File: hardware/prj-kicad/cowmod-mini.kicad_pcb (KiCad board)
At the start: 4 copper layers, 80 x 50 mm, 24 parts, among them P1 PMOD, P2 PMOD, U1 STM32F750V8, U2 ICE40HX1K-VQ100

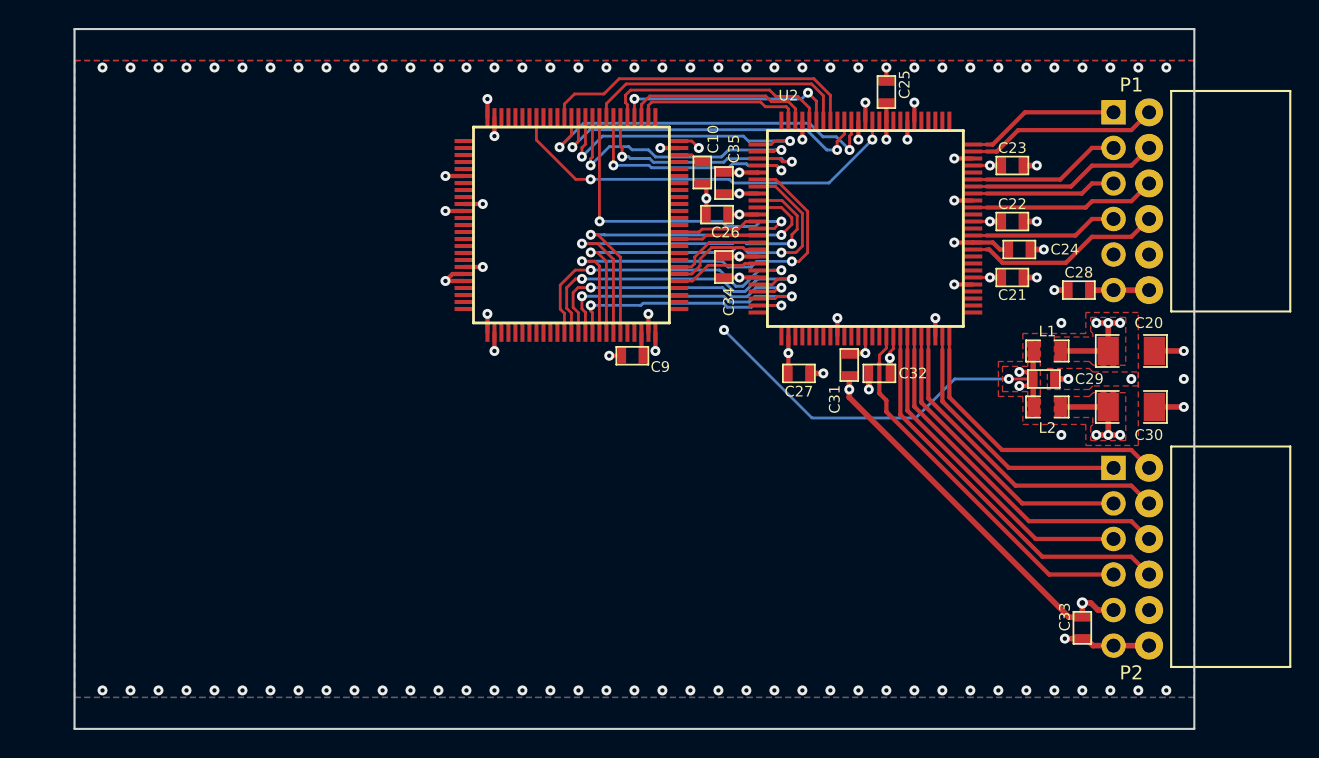
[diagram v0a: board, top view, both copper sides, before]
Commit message: = ADD: Insert ethernet network interface
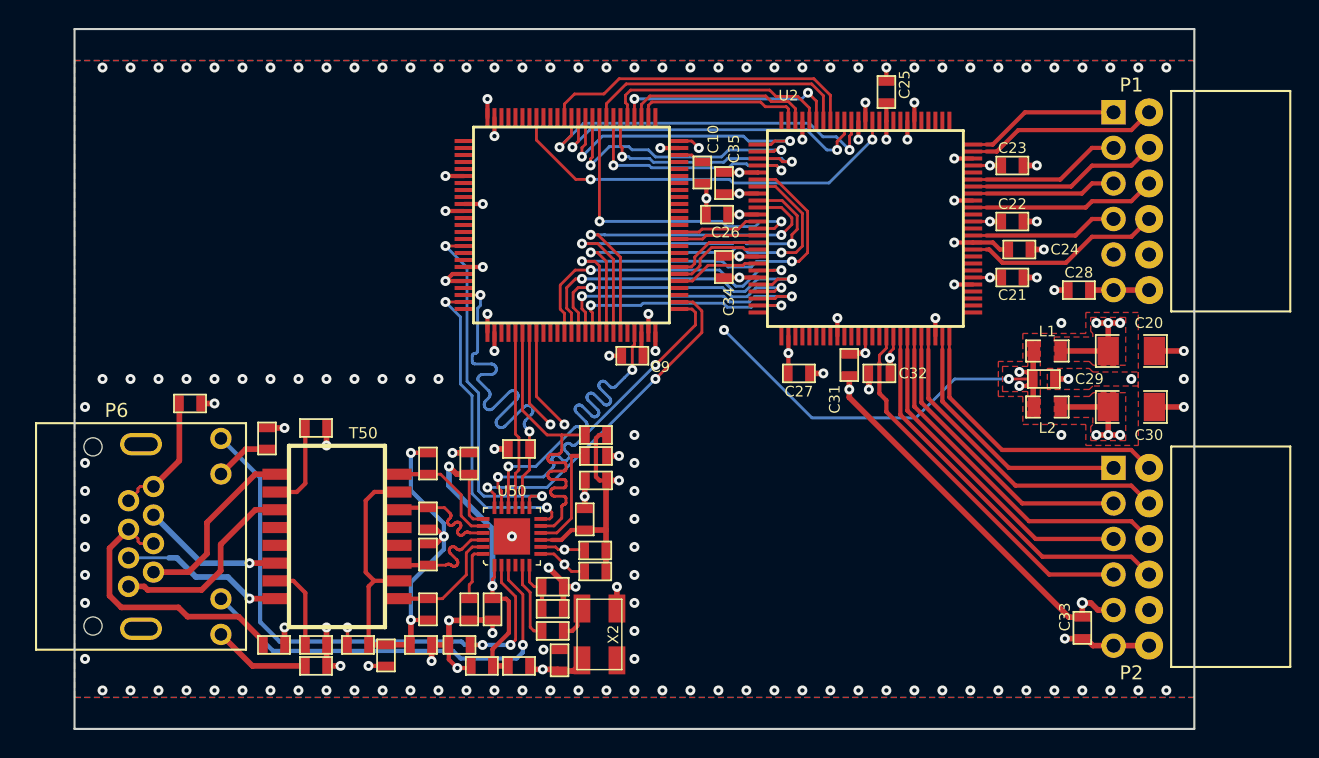
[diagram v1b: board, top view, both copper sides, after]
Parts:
- added C50: 100nF, cartes_v3:SMD0603, F.Cu at (143.2, 125.1)
- added C51: 100nF, cartes_v3:SMD0603, F.Cu at (133.2, 124.0)
- added C52: 100nF, cartes_v3:SMD0603, F.Cu at (128.8, 124.0)
- added C53: 470pF, cartes_v3:SMD0603, F.Cu at (142.7, 119.8)
- added C54: 1uF, cartes_v3:SMD0603, F.Cu at (142.7, 121.4)
- added C55: 1uF, cartes_v3:SMD0603, F.Cu at (137.6, 125.5)
- added C56: 100nF, cartes_v3:SMD0603, F.Cu at (138.4, 121.5)
- added C57: 100nF, cartes_v3:SMD0603, F.Cu at (136.7, 111.0)
- added C58: 1uF, cartes_v3:SMD0603, F.Cu at (145.8, 112.2)
- added C59: 100nF, cartes_v3:SMD0603, F.Cu at (144.9, 115.0)
- added L50: FB100, cartes_v3:SMD0603, F.Cu at (130.8, 124.8)
- added L51: FB120, cartes_v3:SMD0603, F.Cu at (140.2, 125.5)
- added P6: CONN_RJ45, cartes_v3:CONN_615008185121, F.Cu at (113.2, 116.2)
- added R50: 12.1k, cartes_v3:R_0603, F.Cu at (136.7, 121.5)
- added R51: 49.9, cartes_v3:SMD0603, F.Cu at (133.8, 121.5)
- added R52: 49.9, cartes_v3:SMD0603, F.Cu at (133.8, 117.5)
- added R53: 49.9, cartes_v3:SMD0603, F.Cu at (133.8, 115.0)
- added R54: 49.9, cartes_v3:SMD0603, F.Cu at (133.8, 111.0)
- added R55: 75, cartes_v3:SMD0603, F.Cu at (125.8, 108.5)
- added R56: 75, cartes_v3:SMD0603, F.Cu at (125.8, 124.0)
- added R57: 75, cartes_v3:SMD0603, F.Cu at (122.8, 124.0)
- added R58: 75, cartes_v3:SMD0603, F.Cu at (116.8, 106.8)
- added R59: 49.9, cartes_v3:R_0603, F.Cu at (142.7, 123.0)
- added R60: 4.7k, cartes_v3:R_0603, F.Cu at (145.7, 117.2)
- added R61: 4.7k, cartes_v3:R_0603, F.Cu at (145.7, 118.8)
- added R62: 4.7k, cartes_v3:R_0603, F.Cu at (145.8, 109.0)
- added R63: 4.7k, cartes_v3:R_0603, F.Cu at (145.8, 110.5)
- added R64: 4.7k, cartes_v3:R_0603, F.Cu at (140.2, 110.0)
- added R65: 4.7k, cartes_v3:R_0603, F.Cu at (136.0, 124.0)
- added R66: 330, cartes_v3:R_0603, F.Cu at (122.2, 109.2)
- added R67: 330, cartes_v3:R_0603, F.Cu at (125.8, 125.5)
- added T50: TRANSFORMER_1:1, cartes_v3:TR_W749013011, F.Cu at (127.2, 116.2)
- added U50: LAN8742A, cartes_v3:QFN24, F.Cu at (139.8, 116.2)
- added X2: 25MHz, cartes_v3:Q_SMD5x3, F.Cu at (146.0, 123.2)
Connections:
- U1 pad 16: Net-(U1-Pad16) -> ETH_MDC
- U1 pad 23: Net-(U1-Pad23) -> ETH_REF_CLK
- U1 pad 24: Net-(U1-Pad24) -> ETH_MDIO
- U1 pad 30: Net-(U1-Pad30) -> ETH_RST
- U1 pad 31: Net-(U1-Pad31) -> ETH_CRS_DV
- U1 pad 32: Net-(U1-Pad32) -> ETH_RXD0
- U1 pad 33: Net-(U1-Pad33) -> ETH_RXD1
- U1 pad 47: Net-(U1-Pad47) -> ETH_TXEN
- U1 pad 51: Net-(U1-Pad51) -> ETH_TXD0
- U1 pad 52: Net-(U1-Pad52) -> ETH_TXD1
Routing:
- net GND: track 434.3 -> 638.3 mm, vias 112 -> 161
- net +3.3V: track 135.4 -> 214.1 mm, vias 15 -> 19
- net NET_LED2: track 0.00 -> 40.0 mm, vias 0 -> 2
- net Net-(C51-Pad1): track 0.00 -> 38.9 mm, vias 0 -> 3
- net NET_LED1: track 0.00 -> 30.2 mm, vias 0 -> 1
- net ETH_REF_CLK: track 0.00 -> 29.4 mm, vias 0 -> 2
- net ETH_RXD1: track 0.00 -> 28.7 mm, vias 0 -> 2
- net ETH_RXD0: track 0.00 -> 28.4 mm, vias 0 -> 2
- net ETH_MDC: track 0.00 -> 26.1 mm, vias 0 -> 2
- net Net-(C55-Pad1): track 0.00 -> 25.5 mm, vias 0 -> 2
- net ETH_TXD0: track 0.00 -> 25.0 mm, vias 0 -> 2
- net ETH_TXD1: track 0.00 -> 25.0 mm, vias 0 -> 2
- net ETH_TXEN: track 0.00 -> 25.0 mm, vias 0 -> 2
- net ETH_CRS_DV: track 0.00 -> 24.5 mm
- net ETH_MDIO: track 0.00 -> 23.2 mm, vias 0 -> 2
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- added copper zone on In2.Cu, net +3.3V
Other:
- net class Default: via_dia 0.8 -> 0.6
- rule solder_mask_min_width: 0.25 -> 0.05
- rule trace_min: 0.2032 -> 0.1524
- board text removed: "PWR"

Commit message: = ADD: Insert power supply regulators (3V3 / 1V2 / 2V5)
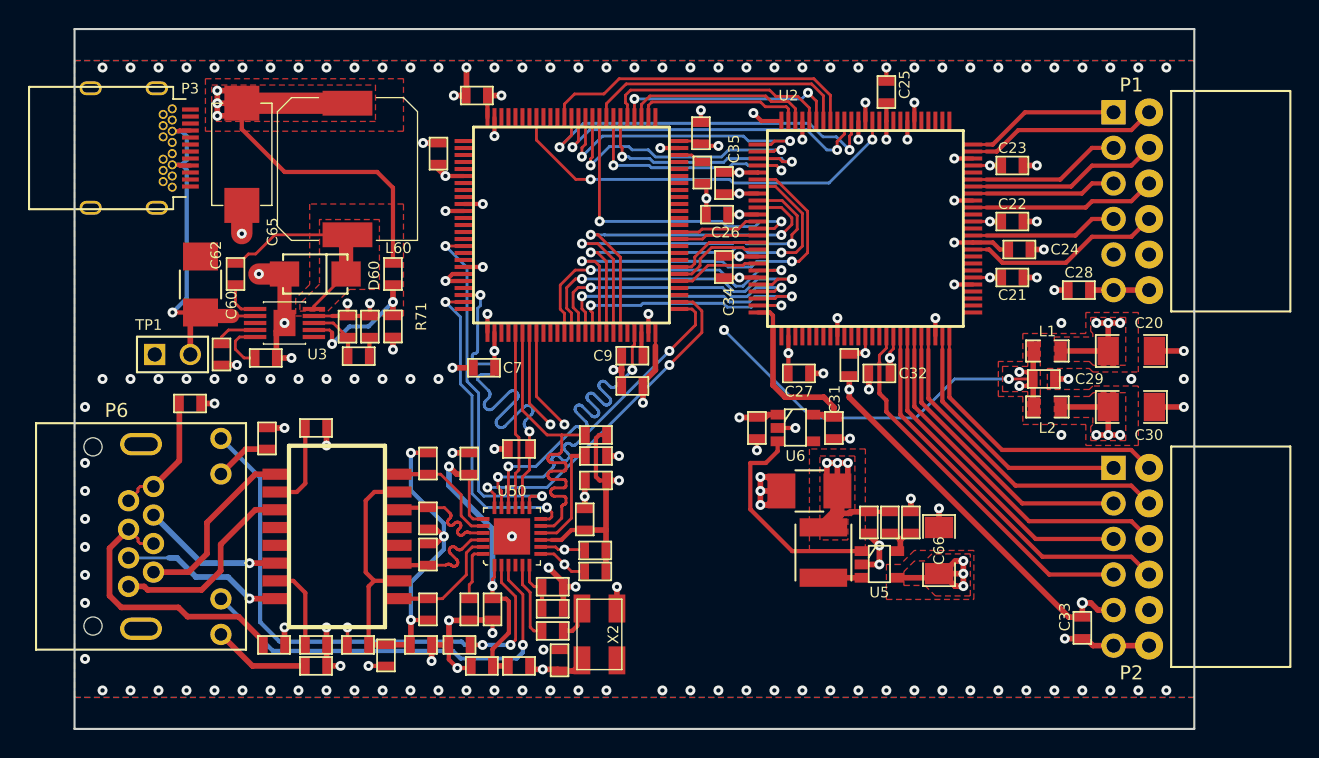
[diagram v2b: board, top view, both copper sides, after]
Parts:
- added C4: 100nF, cowmod-mini:SMD0603, F.Cu at (148.3, 105.5)
- added C5: 100nF, cowmod-mini:SMD0603, F.Cu at (134.5, 88.9)
- added C6: 100nF, cowmod-mini:SMD0603, F.Cu at (153.2, 87.4)
- added C60: 2,2uF, cartes_v3:C_1210, F.Cu at (117.5, 98.2)
- added C61: 10nF, cartes_v3:SMD0603, F.Cu at (119.0, 103.2)
- added C62: 100nF, cartes_v3:C_0603, F.Cu at (120.0, 97.5)
- added C63: n/a, cartes_v3:SMD0603, F.Cu at (128.0, 101.3)
- added C64: 4,7nF, cartes_v3:SMD0603, F.Cu at (129.6, 101.3)
- added C65: 220uF, cartes_v3:C_TPB_D4, F.Cu at (120.5, 89.0)
- added C66: 10uF, cowmod-mini:SMD1206, F.Cu at (170.3, 117.3)
- added C67: C, cowmod-mini:SMD0603, F.Cu at (165.2, 115.2)
- added C68: 47uF, cowmod-mini:C_1210, F.Cu at (161.0, 113.0)
- added C69: 1uF, cowmod-mini:SMD0603, F.Cu at (157.2, 108.5)
- added C7: 100nF, cowmod-mini:SMD0603, F.Cu at (137.8, 104.2)
- added C70: 1uF, cowmod-mini:SMD0603, F.Cu at (162.8, 108.5)
- added C8: 100nF, cowmod-mini:SMD0603, F.Cu at (137.2, 84.8)
- added D60: MBRA340, cartes_v3:DO214AC, F.Cu at (125.7, 97.5)
- added L60: 27uH, cartes_v3:I_MSS1048, F.Cu at (128.0, 90.0)
- added L61: 4,7uH, cowmod-mini:I_TYS4012, F.Cu at (162.0, 117.4)
- added P3: CONN_USB-C, cowmod-mini:CONN_632723300011, F.Cu at (114.8, 88.5)
- added R68: 100k, cartes_v3:R_0603, F.Cu at (122.2, 103.5)
- added R69: 20k, cartes_v3:R_0603, F.Cu at (128.8, 103.4)
- added R70: 47k, cartes_v3:R_0603, F.Cu at (131.2, 97.5)
- added R71: 15k, cartes_v3:R_0603, F.Cu at (131.2, 101.2)
- added R72: R, cowmod-mini:SMD0603, F.Cu at (166.8, 115.2)
- added R73: R, cowmod-mini:SMD0603, F.Cu at (168.2, 115.2)
- added TP1: CONN_2, cowmod-mini:CONN_2, F.Cu at (115.5, 103.2)
- added U3: TPS54160A, cartes_v3:MSOP10p, F.Cu at (123.5, 101.0)
- added U5: TPS560200, cowmod-mini:SOT23-5, F.Cu at (166.0, 118.2)
- added U6: LD6815, cowmod-mini:SOT23-5, F.Cu at (160.0, 108.5)
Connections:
- U2 pad 50: Net-(U2-Pad50) -> +3.3V
- U2 pad 75: Net-(U2-Pad75) -> +2.5V
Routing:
- net +3.3V: track 214.1 -> 355.0 mm, vias 19 -> 27
- net GND: track 638.3 -> 713.8 mm, vias 161 -> 173
- net +VBUS: track 0.00 -> 27.1 mm, vias 0 -> 1
- net /Power Supply/3V3_SW: track 0.00 -> 15.8 mm
- net 1V2_EN: track 0.00 -> 15.5 mm
- net +1.2V: track 46.3 -> 61.2 mm, vias 4 -> 7
- net +2.5V: track 0.00 -> 13.4 mm
- net Net-(R70-Pad2): track 0.00 -> 10.0 mm, vias 0 -> 2
- net Net-(C63-Pad1): track 0.00 -> 4.19 mm
- net Net-(R68-Pad1): track 0.00 -> 3.78 mm
- net Net-(C61-Pad1): track 0.00 -> 3.10 mm
- net Net-(C62-Pad1): track 0.00 -> 2.90 mm
- net Net-(R72-Pad2): track 0.00 -> 2.80 mm
- net Net-(L61-Pad1): track 0.00 -> 2.73 mm
- net Net-(C64-Pad1): track 0.00 -> 1.36 mm
- added copper zone on F.Cu, net +1.2V
- added copper zone on F.Cu, net /Power Supply/3V3_SW
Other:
- net class Default: clearance 0.1524 -> 0.1
- rule trace_clearance: 0.1524 -> 0.1
- rule trace_min: 0.1524 -> 0.1

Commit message: = ADD: Insert an SPI flash for MCU
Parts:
- added U4: M25P16-VME, cowmod-mini:SOIC-8E, F.Cu at (152.5, 111.0)
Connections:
- U1 pad 1: Net-(U1-Pad1) -> MEM_IO2
- U1 pad 36: Net-(U1-Pad36) -> MEM_CLK
- U1 pad 59: Net-(U1-Pad59) -> MEM_IO1
- U1 pad 60: Net-(U1-Pad60) -> MEM_IO3
- U1 pad 66: Net-(U1-Pad66) -> MEM_IO0
- U1 pad 92: Net-(U1-Pad92) -> MEM_CS
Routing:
- net MEM_IO2: track 0.00 -> 30.3 mm, vias 0 -> 2
- net MEM_IO3: track 0.00 -> 30.0 mm, vias 0 -> 2
- net MEM_IO0: track 0.00 -> 30.0 mm, vias 0 -> 3
- net MEM_CLK: track 0.00 -> 30.0 mm
- net MEM_IO1: track 0.00 -> 30.0 mm, vias 0 -> 2
- net MEM_CS: track 0.00 -> 26.5 mm, vias 0 -> 2
- net GND: track 713.8 -> 739.6 mm, vias 173 -> 177
- net +3.3V: track 355.0 -> 355.6 mm, vias 27 -> 28

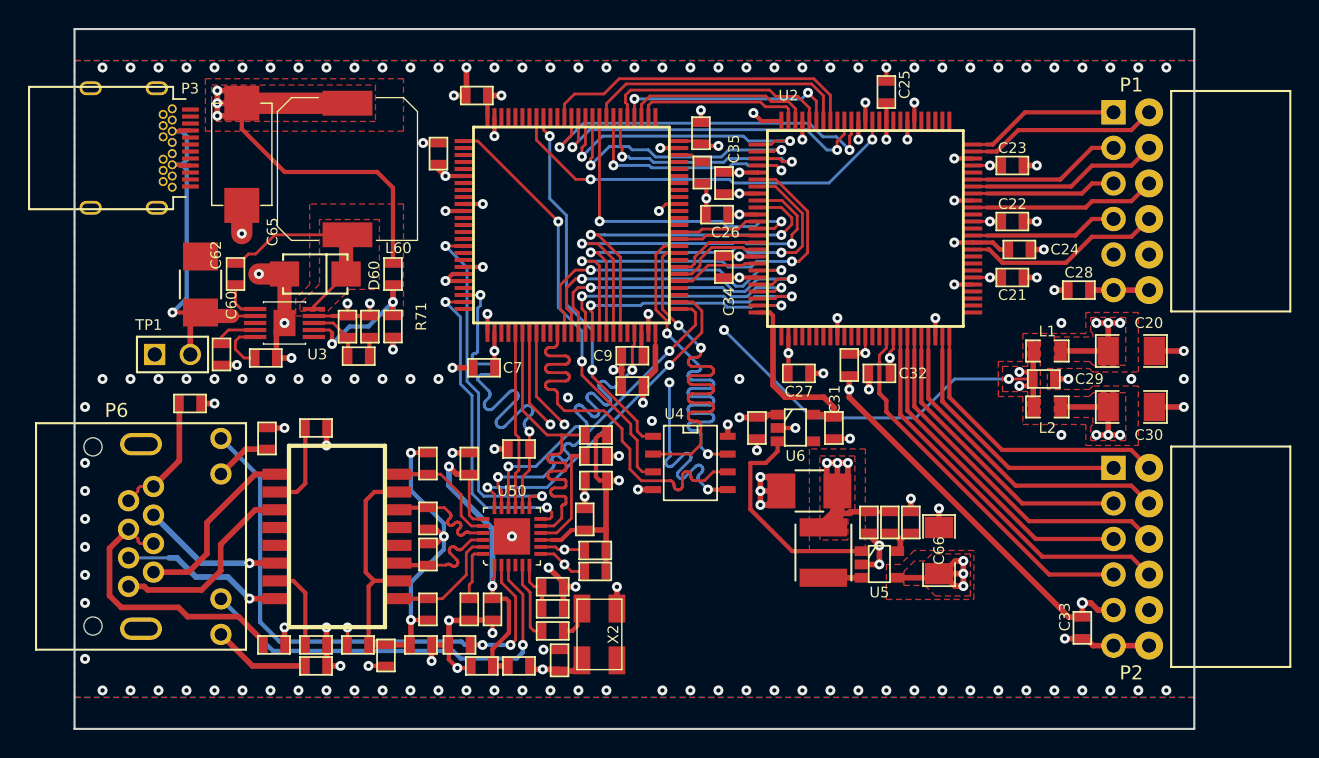
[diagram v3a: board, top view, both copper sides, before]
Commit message: = UPD: Add missing reset circuit, debug port and simple UART console
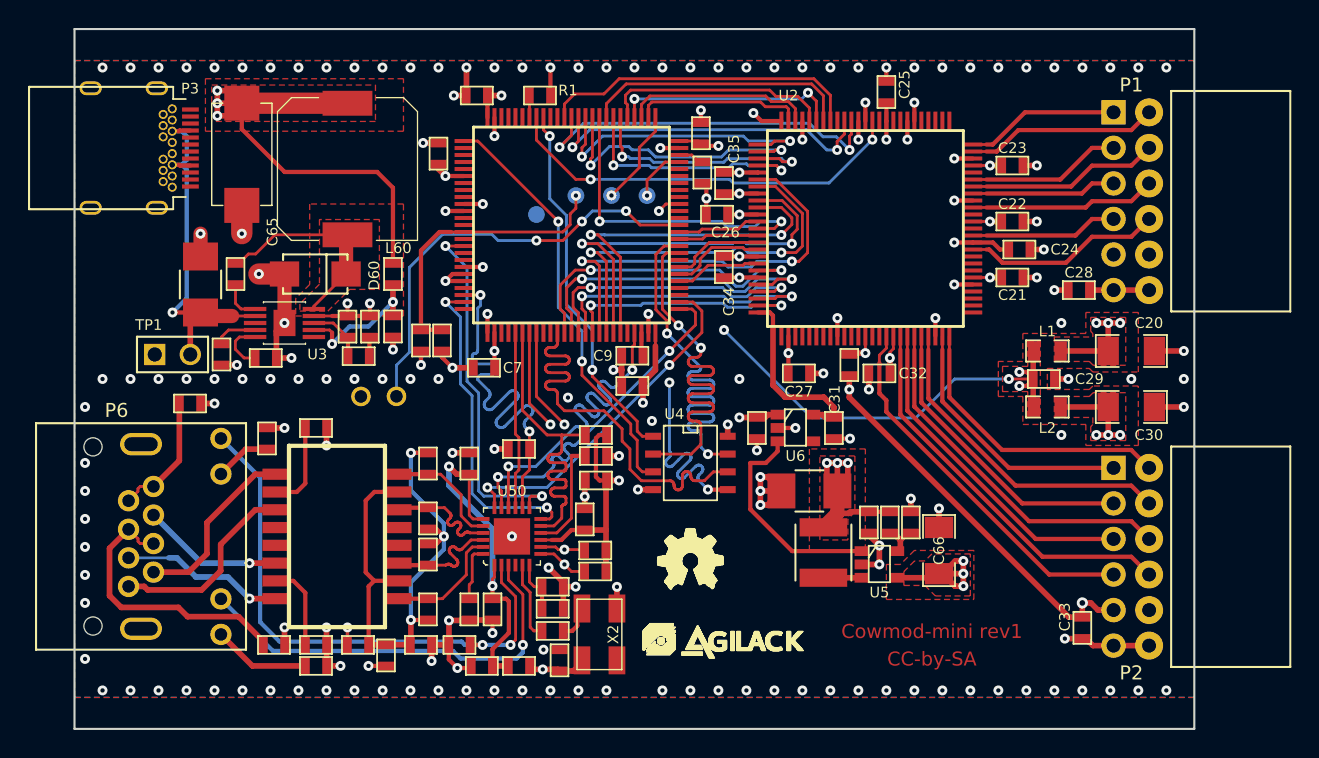
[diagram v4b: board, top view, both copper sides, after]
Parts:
- added C1: 1uF, cowmod-mini:SMD0603, F.Cu at (134.8, 102.2)
- added R1: 10k, cowmod-mini:SMD0603, F.Cu at (141.8, 84.8)
- added R2: 10k, cowmod-mini:SMD0603, F.Cu at (133.2, 102.2)
- added TP10: CONN_1, cowmod-mini:TP_PIN, F.Cu at (131.5, 106.2)
- added TP11: CONN_1, cowmod-mini:TP_PIN, F.Cu at (129.0, 106.2)
- added TP2: CONN_1, cowmod-mini:TP_SMD, B.Cu at (146.9, 91.9)
- added TP3: CONN_1, cowmod-mini:TP_SMD, B.Cu at (149.4, 91.9)
- added TP4: CONN_1, cowmod-mini:TP_SMD, B.Cu at (144.3, 91.9)
- added TP5: CONN_1, cowmod-mini:TP_SMD, B.Cu at (141.5, 93.2)
- added agilack-11.5: 450px, cowmod-mini:logo-agilack-11.5, F.Cu at (155.2, 123.8)
- added ohw_logo: VAL**, cowmod-mini:logo-ohw, F.Cu at (152.5, 118.0)
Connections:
- U1 pad 14: Net-(U1-Pad14) -> RST
- U1 pad 72: Net-(U1-Pad72) -> SWD_IO
- U1 pad 76: Net-(U1-Pad76) -> SWD_CLK
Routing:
- net Net-(TP10-Pad1): track 0.00 -> 31.3 mm, vias 0 -> 3
- net RST: track 0.00 -> 20.8 mm, vias 0 -> 1
- net GND: track 739.6 -> 747.7 mm, vias 177 -> 178
- net +3.3V: track 355.6 -> 363.3 mm, vias 28 -> 29
- net SWD_CLK: track 0.00 -> 6.87 mm, vias 0 -> 1
- net SWD_IO: track 0.00 -> 3.92 mm, vias 0 -> 1
- net Net-(R1-Pad1): track 0.00 -> 1.58 mm
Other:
- board text added: "CC-by-SA"
- board text added: "Cowmod-mini rev1"
